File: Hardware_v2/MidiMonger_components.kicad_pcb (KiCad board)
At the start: 2 copper layers, 40 x 100 mm, 67 parts, among them J1 Conn_01x09_Male, J2 Conn_01x09_Male, J3 Conn_01x08_Male, J4 Conn_01x08_Male, J5 SWD_Header, J6 Eurorack_10_pin_power, J7 UART_Test, U1 STM32F446RETx, U2 TL074, U3 74HCT244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

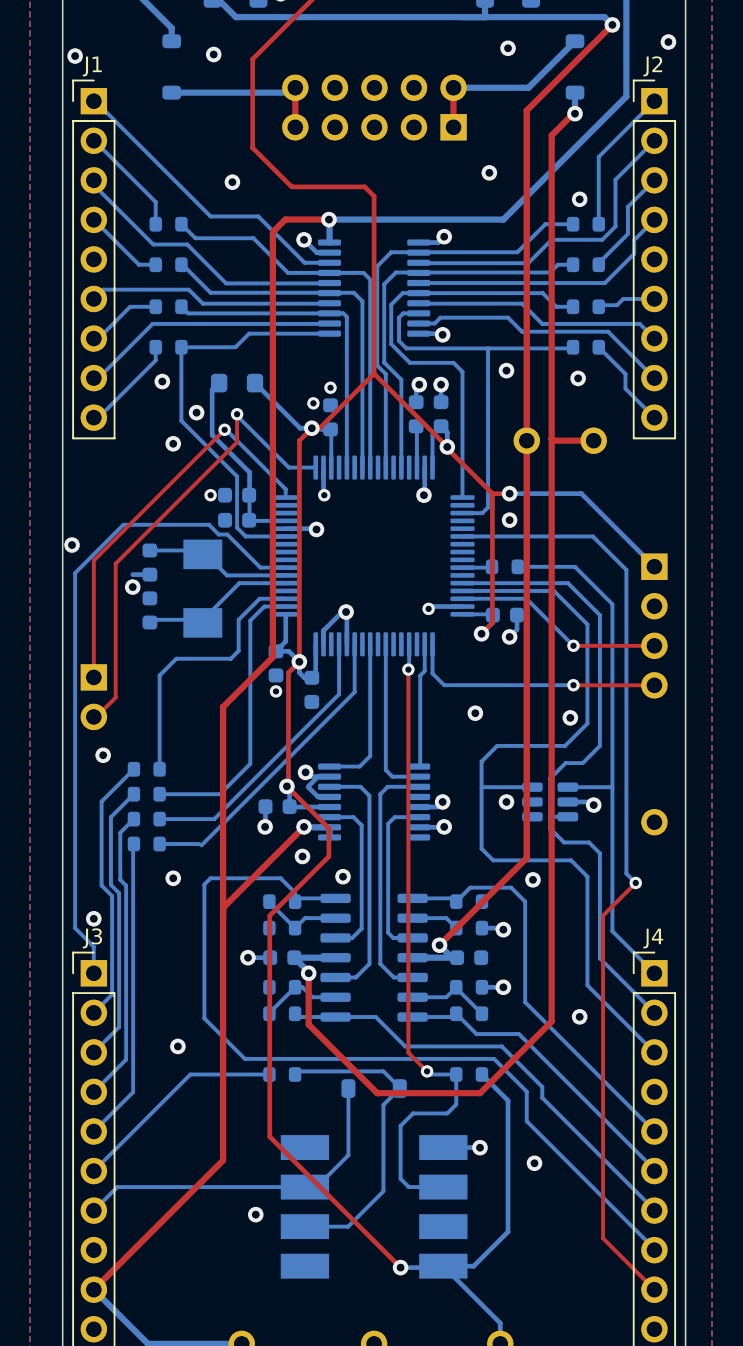
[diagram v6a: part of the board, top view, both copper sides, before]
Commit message: Added additional decoupling capacitors to 5V line
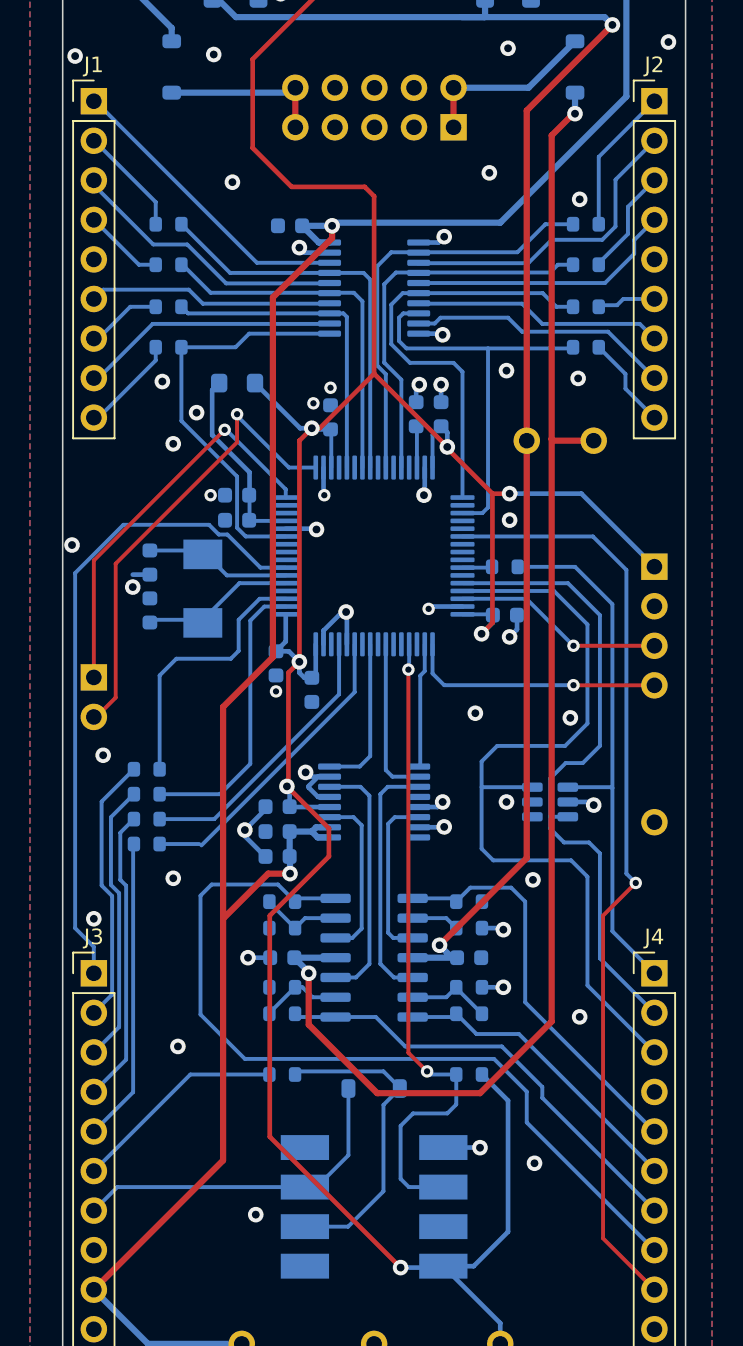
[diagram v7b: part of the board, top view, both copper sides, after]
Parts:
- added C18: 100nF, Capacitor_SMD:C_0603_1608Metric, B.Cu at (113.8, 114.9)
- added C20: 4.7uF, Capacitor_SMD:C_0603_1608Metric, B.Cu at (113.8, 116.5)
- added C21: 100nF, Capacitor_SMD:C_0603_1608Metric, B.Cu at (114.6, 76.0)
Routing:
- net GND: track 45.7 -> 48.8 mm, vias 66 -> 64
- net +5V: track 147.0 -> 149.5 mm
- net /CV4_OUT: track 54.6 -> 53.8 mm
